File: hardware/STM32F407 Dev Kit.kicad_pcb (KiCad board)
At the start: 2 copper layers, 153 parts, among them J1 GMSB0531112YEU, J10 Conn_01x04, J11 TBC 2.54mm 10A, J12 IMP34DT05, J2 Conn_01x06, J3 RJMG1S8008101BR, J4 B2B-XH-A(LF)(SN), J5 Conn_01x04, J7 SJ-3524-SMT, J8 GMSB0531112YEU, J9 Conn_01x04, SW1 SW TACT-SPST, SW2 SW TACT-SPST, SW3 SW TACT-SPST, U1 STM32F103CBT6, U2 DP83826IRHBR, U3 DRV8701ERGET, U4 DMHT6016LFJ-13, U5 ADS122C04IPW, U6 CS43L22, U7 STM32F407VGT6, U8 AP63203WU, U9 XC6206P182MR, Y1 ABM8G-8.000MHZ-18-D2Y-T, Y2 ABM8G-25.000MHZ-9-B4Y-T, Y3 ABM8G-8.000MHZ-18-D2Y-T

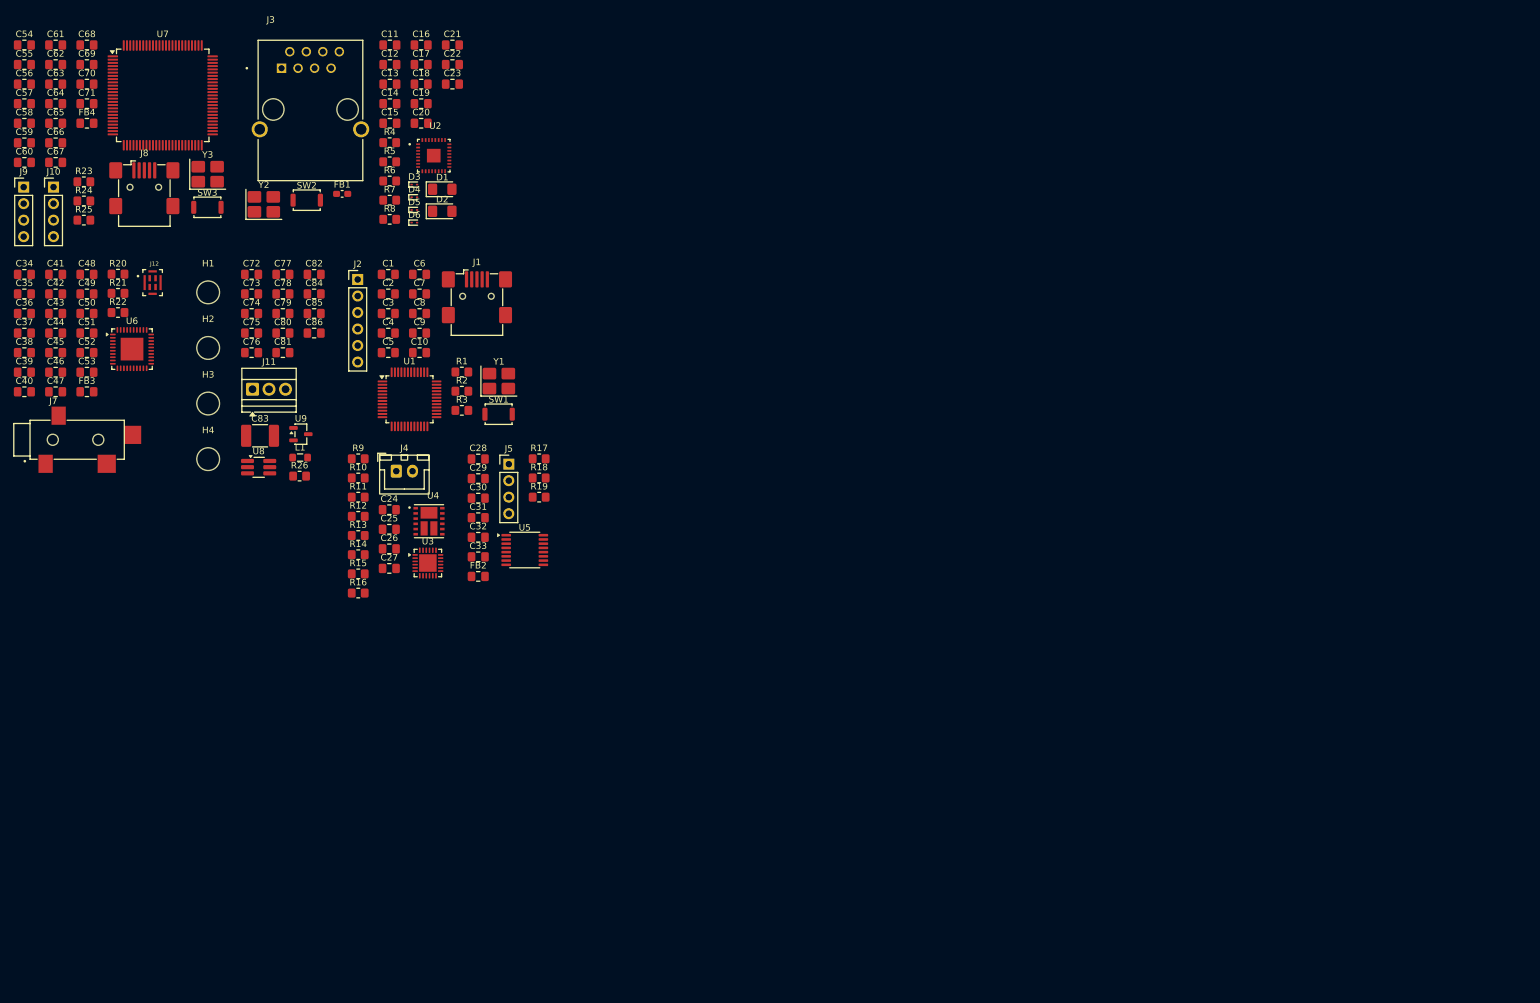
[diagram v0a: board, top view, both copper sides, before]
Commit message: Draw Board Outline
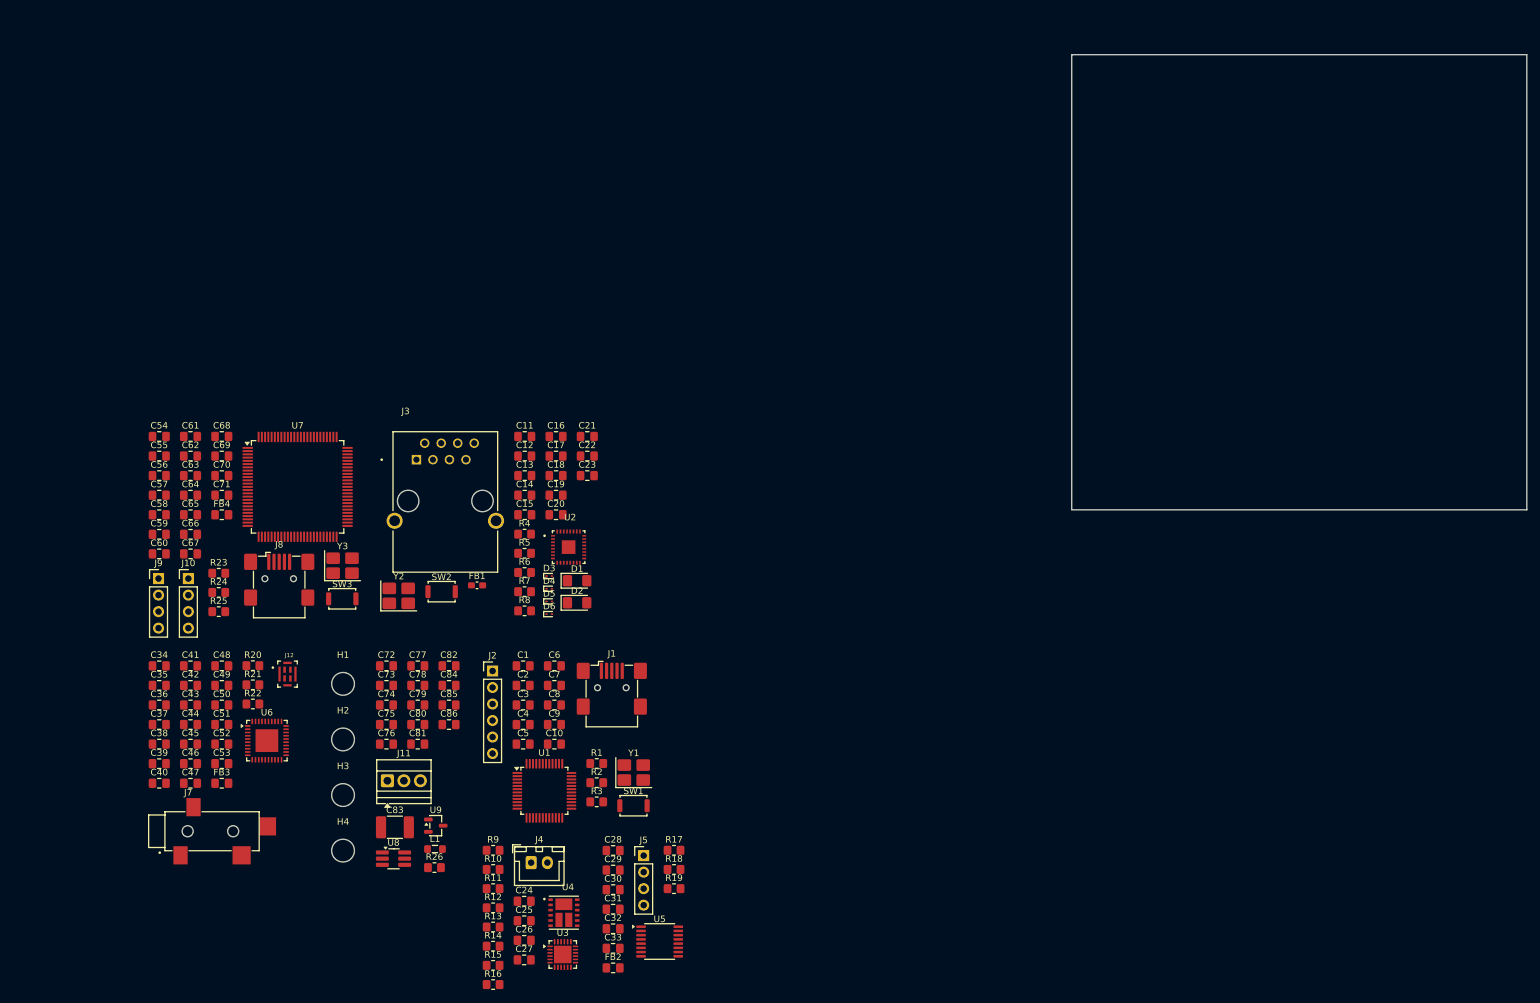
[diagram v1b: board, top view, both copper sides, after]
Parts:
- moved C39 63.7 mm to (44.6, 129.1)
- moved C46 63.7 mm to (49.5, 129.1)
- moved C53 63.7 mm to (54.3, 129.1)
- moved C83 63.7 mm to (80.9, 138.8)
- moved U9 63.7 mm to (87.2, 138.6)
- moved C1 63.7 mm to (100.6, 114.0)
- moved C10 63.7 mm to (105.4, 126.0)
- moved C11 63.7 mm to (100.9, 78.7)
- moved C12 63.7 mm to (100.9, 81.7)
- moved C14 63.7 mm to (100.9, 87.8)
- moved C15 63.7 mm to (100.9, 90.8)
- moved C16 63.7 mm to (105.7, 78.7)
- moved C17 63.7 mm to (105.7, 81.7)
- moved C19 63.7 mm to (105.7, 87.8)
- moved C2 63.7 mm to (100.6, 117.0)
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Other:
- board outline added: 70 x 70 mm

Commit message: Place Components for Ethernet
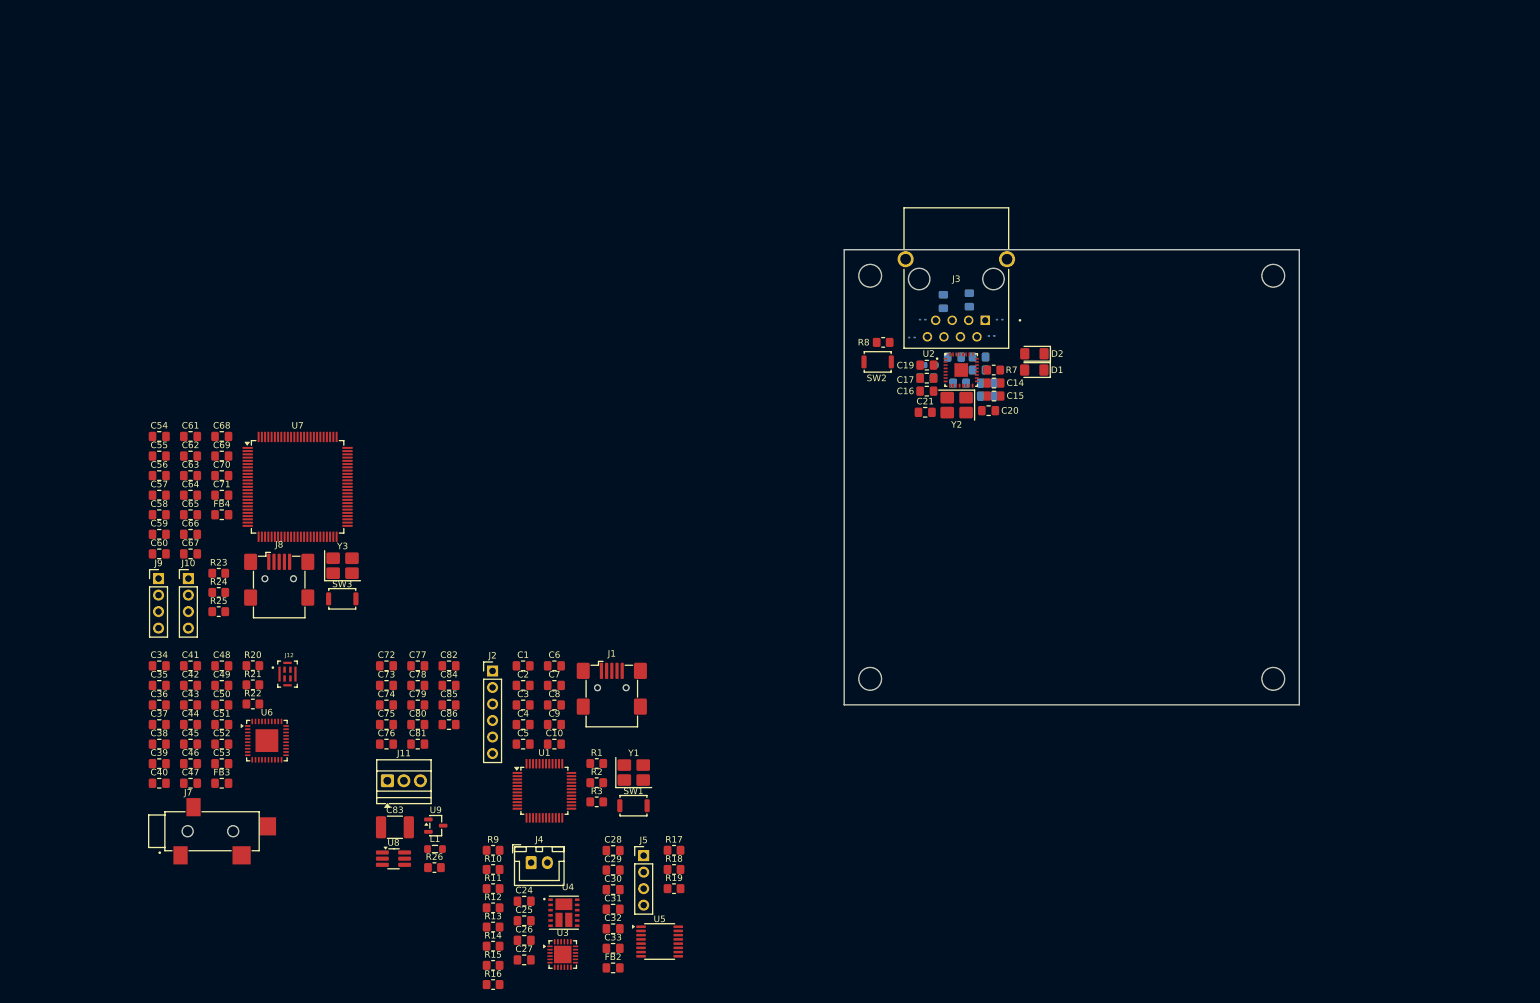
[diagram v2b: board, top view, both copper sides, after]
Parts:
- C11, C12, C13, C18, C22, C23, D3, D4, D5, D6, FB1, R4, R5, R6: moved to B.Cu
- moved H2 159.9 mm to (216.0, 54.0)
- moved H3 144.2 mm to (216.0, 116.0)
- moved H1 102.5 mm to (154.0, 54.0)
- moved Y2 90.7 mm to (167.3, 73.9), turned to 180 degrees
- moved J3 85.7 mm to (167.2, 54.5), turned to 180 degrees
- moved H4 85.3 mm to (154.0, 116.0)
- moved D2 80.1 mm to (179.3, 66.0), turned to 180 degrees
- moved R7 79.8 mm to (173.0, 68.5), turned to 180 degrees
- moved D3 79.7 mm to (173.9, 60.8)
- moved D4 78.4 mm to (172.7, 63.2)
- moved D1 77.4 mm to (179.2, 68.5), turned to 180 degrees
- moved FB1 77.4 mm to (163.1, 67.8), turned to 180 degrees
- moved R6 77.4 mm to (170.8, 66.5)
- moved SW2 75.8 mm to (155.2, 67.2)
- moved R5 75.4 mm to (170.8, 68.5)
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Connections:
- C12 pad 1: VDDIO -> +3V3
- C13 pad 1: VDDIO -> +3V3
- C14 pad 1: VDDIO -> +3V3
- C15 pad 1: VDDIO -> +3V3
- C16 pad 1: VDDA3V3 -> Net-(U2-VDDA3V3)
- C17 pad 1: VDDA3V3 -> Net-(U2-VDDA3V3)
- C18 pad 1: VDDA3V3 -> Net-(U2-VDDA3V3)
- C19 pad 1: VDDA3V3 -> Net-(U2-VDDA3V3)
- FB1 pad 2: VDDA3V3 -> +3V3
- R7 pad 1: VDDIO -> +3V3
- R8 pad 1: VDDIO -> +3V3
- U2 pad 17: VDDIO -> +3V3

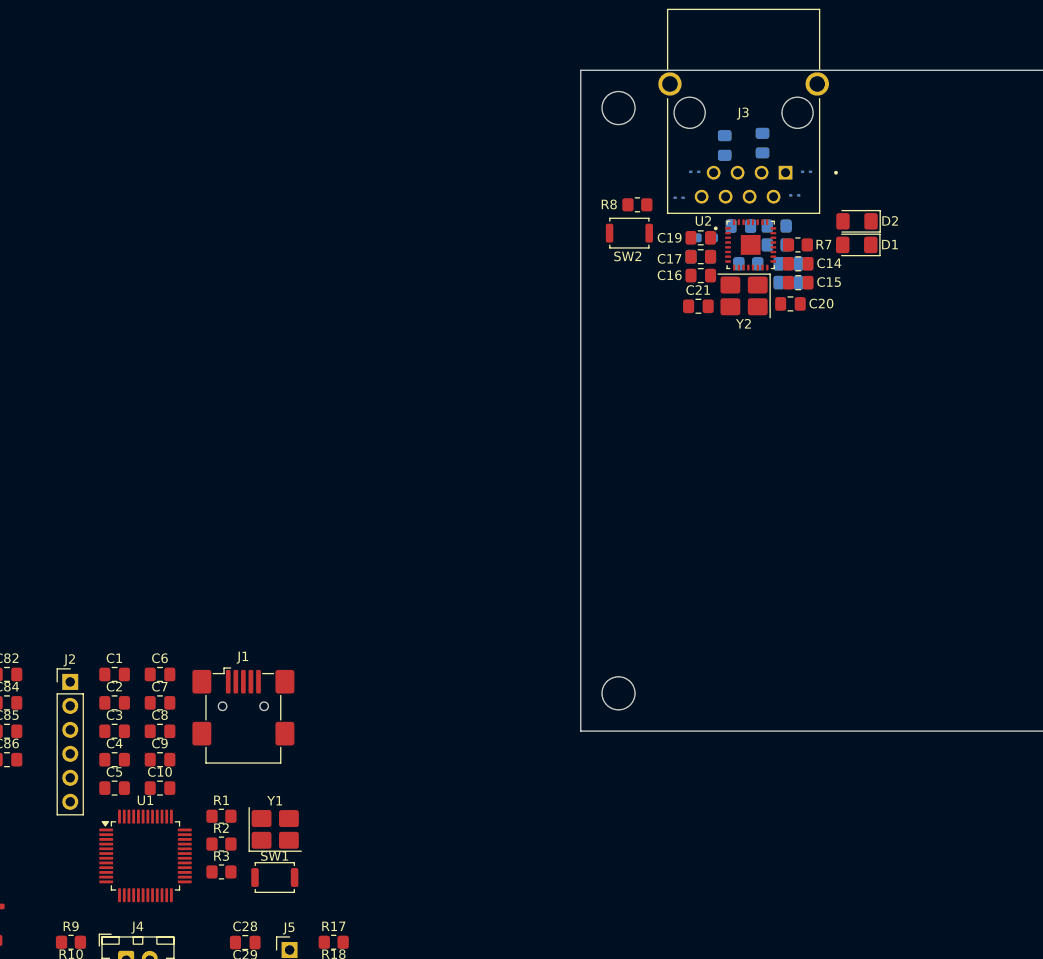
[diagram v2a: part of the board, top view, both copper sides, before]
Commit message: Place components for STM32F103 Programmer/Debugger
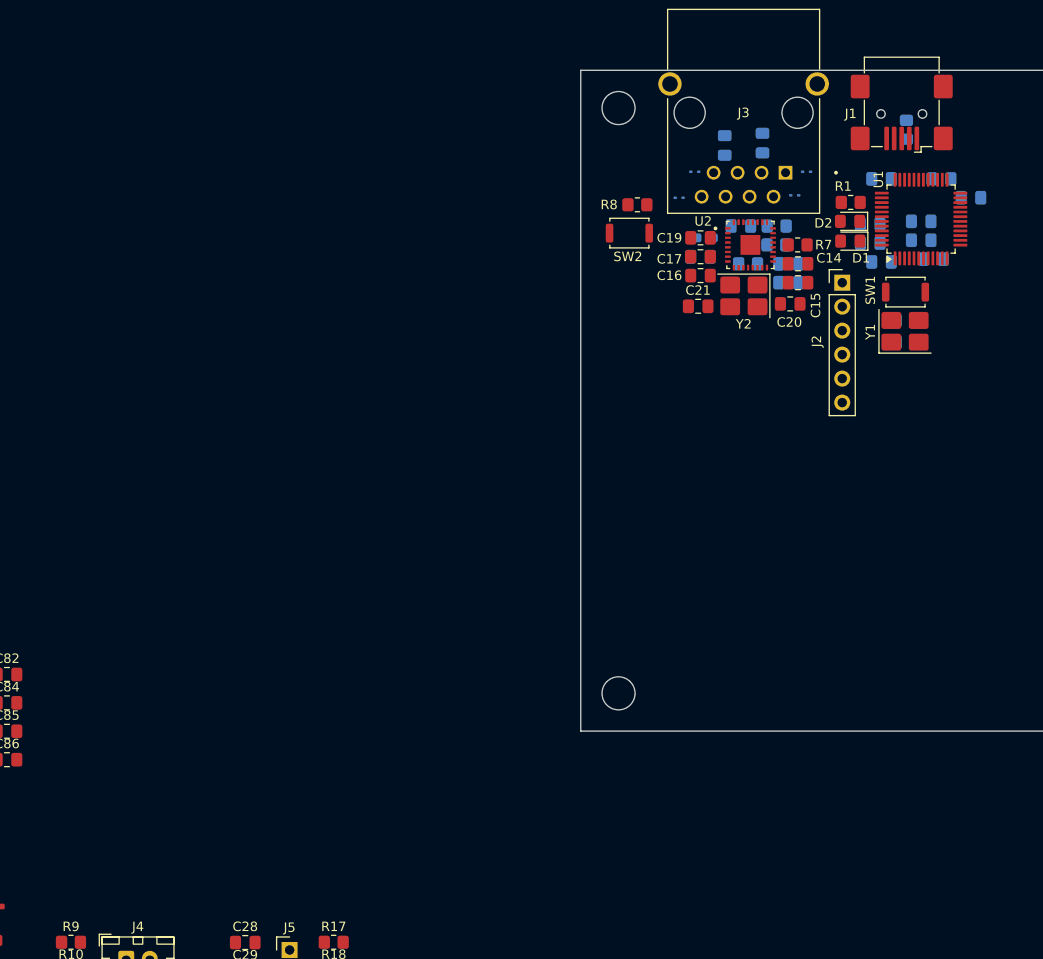
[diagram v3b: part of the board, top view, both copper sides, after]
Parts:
- C1, C10, C2, C3, C4, C5, C6, C7, C8, C9, R2, R3: moved to B.Cu
- D1, D2: footprint STM32F407 Dev Kit Library:LED_1206_3216Metric_Pad1.42x1.75mm_HandSolder -> STM32F407 Dev Kit Library:LED_0805_2012Metric_Pad1.15x1.40mm_HandSolder
- moved C5 110.2 mm to (191.3, 63.5)
- moved R3 107.0 mm to (184.5, 56.3), turned to -90 degrees
- moved U1 106.3 mm to (186.1, 65.8), turned to 90 degrees
- moved R2 103.8 mm to (188.2, 61.5), turned to 180 degrees
- moved C4 101.9 mm to (181.9, 61.5), turned to 180 degrees
- moved C1 97.3 mm to (187.4, 70.0)
- moved C8 97.1 mm to (186.1, 66.0), turned to 180 degrees
- moved C3 95.3 mm to (180.7, 68.3), turned to 180 degrees
- moved C2 94.8 mm to (180.7, 66.3), turned to 180 degrees
- moved C7 94.4 mm to (186.1, 68.0), turned to 180 degrees
- moved J1 93.8 mm to (184.0, 54.6), turned to 180 degrees
- moved C10 93.3 mm to (184.5, 76.5)
- moved R1 93.1 mm to (178.6, 64.0), turned to 180 degrees
- moved J2 92.1 mm to (177.7, 72.5)
- moved SW1 91.2 mm to (184.4, 73.5)
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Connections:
- R2 pad 2: Net-(U1-PB15) -> /[3] - STM32F103 debugger/F407_JTMS
- U1 pad 28: Net-(U1-PB15) -> unconnected-(U1-PB15-Pad28)

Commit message: Place components for Power section
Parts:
- C75, C76, C80, C81, C83, R26: moved to B.Cu
- moved U8 143.6 mm to (198.7, 61.8), turned to 180 degrees
- moved C74 143.3 mm to (206.1, 52.6), turned to -90 degrees
- moved C75 142.9 mm to (204.0, 52.6), turned to -90 degrees
- moved C83 142.5 mm to (196.2, 55.0), turned to 180 degrees
- moved J11 140.9 mm to (195.7, 51.6)
- moved R26 140.7 mm to (197.5, 58.0), turned to 180 degrees
- moved C80 140.6 mm to (206.1, 52.6), turned to -90 degrees
- moved C78 135.8 mm to (204.0, 52.6), turned to -90 degrees
- moved L1 135.2 mm to (197.7, 64.4)
- moved C73 135.0 mm to (201.5, 58.9)
- moved C81 134.9 mm to (203.7, 63.1)
- moved C72 134.6 mm to (201.5, 56.8)
- moved C76 133.8 mm to (196.9, 61.7), turned to -90 degrees
- moved C79 132.2 mm to (203.7, 63.1)
- moved C77 130.6 mm to (203.7, 61.0)
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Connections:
- J11 pad 1: +12V -> GND
- J11 pad 3: GND -> +12V
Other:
- board size 70 x 70 mm -> 65.2 x 70 mm

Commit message: Place components for Motor Driver
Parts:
- C24, C25, C26, L1, R11, R13, R14, R15, R16: moved to B.Cu
- moved R16 144.1 mm to (205.5, 69.4), turned to 180 degrees
- moved C27 135.4 mm to (197.6, 64.5), turned to 180 degrees
- moved R15 132.3 mm to (194.2, 71.4)
- moved R12 132.3 mm to (197.6, 66.5)
- moved C26 132.1 mm to (197.6, 66.3), turned to 180 degrees
- moved J4 131.9 mm to (211.3, 70.7), turned to 90 degrees
- moved R14 131.7 mm to (194.2, 69.4)
- moved C25 130.2 mm to (199.5, 68.3), turned to 180 degrees
- moved R11 128.1 mm to (193.7, 65.4)
- moved U4 128.0 mm to (204.8, 69.5), turned to 90 degrees
- moved R13 127.1 mm to (194.2, 73.4), turned to 180 degrees
- moved U3 126.8 mm to (198.1, 70.4), turned to -90 degrees
- moved R10 125.1 mm to (199.0, 74.3)
- moved C24 124.4 mm to (193.7, 67.4), turned to 180 degrees
- moved R9 120.3 mm to (195.2, 74.3)
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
